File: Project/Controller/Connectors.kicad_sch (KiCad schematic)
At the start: 24 parts, among them J10 Servo, J11 Servo, J12 Servo, J13 Thruster, J14 I2C, J15 I2C, J16 UART1, J17 UART2, J18 SPI1, J19 SPI2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

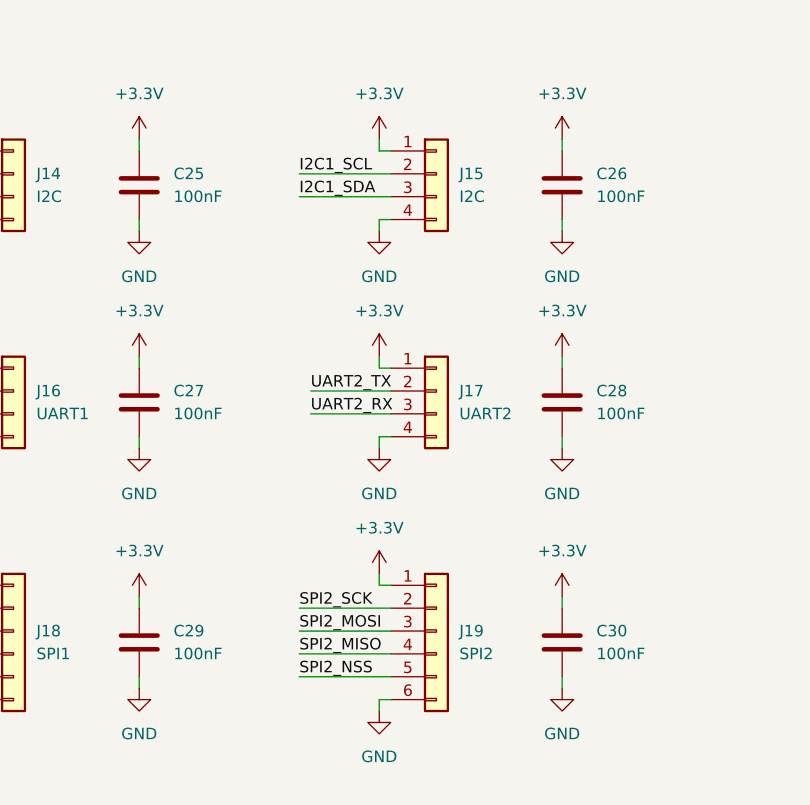
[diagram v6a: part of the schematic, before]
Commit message: Re-annotate symbols
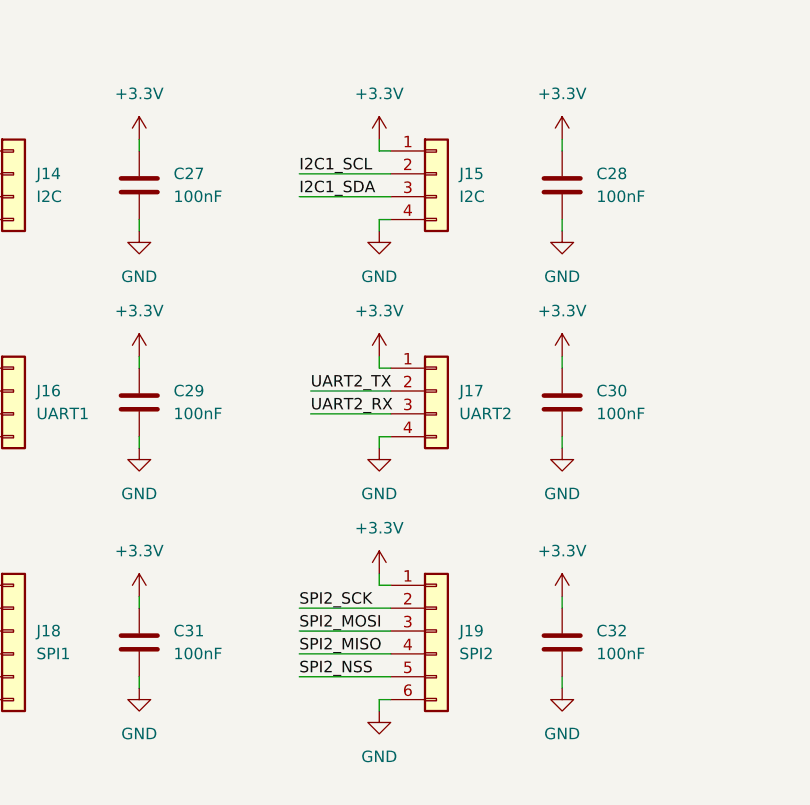
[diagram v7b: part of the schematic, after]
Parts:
- renumbered C25 to C27, C26 to C28, C27 to C29, C28 to C30, C29 to C31, C30 to C32

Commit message: Add SHTC3 humidity sensor
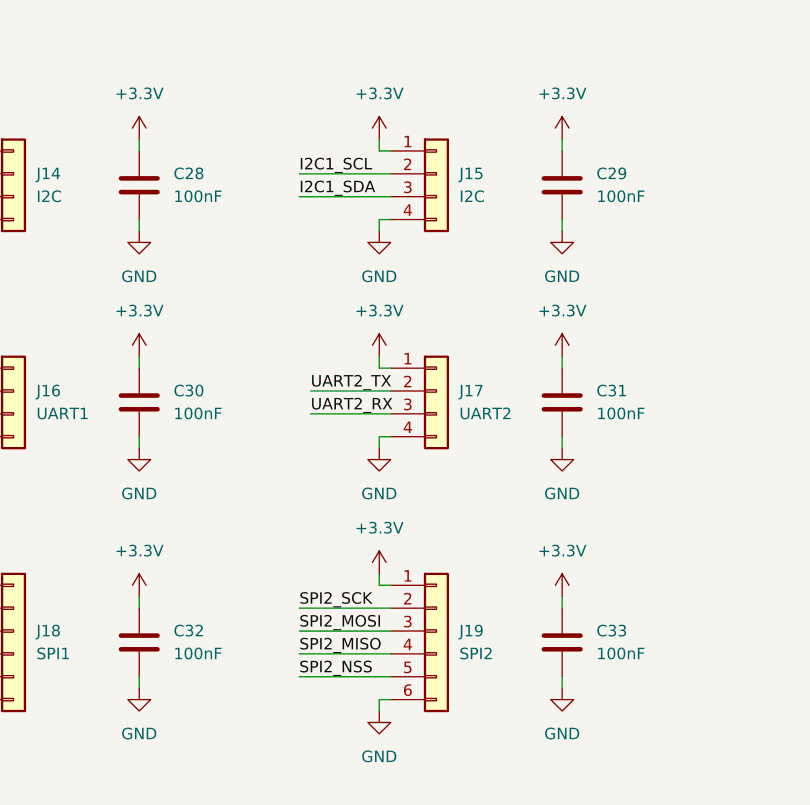
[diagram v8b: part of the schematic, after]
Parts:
- renumbered C27 to C28, C28 to C29, C29 to C30, C30 to C31, C31 to C32, C32 to C33
